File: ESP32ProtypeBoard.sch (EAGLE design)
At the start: 97 parts, among them IC1 SOIC-8, IC2 SI4431BDY, J10 POWER_JACKPTH_LOCK, Q2 MMBT3904, Q3 MMBT3904, U2 ESP-WROOM-32

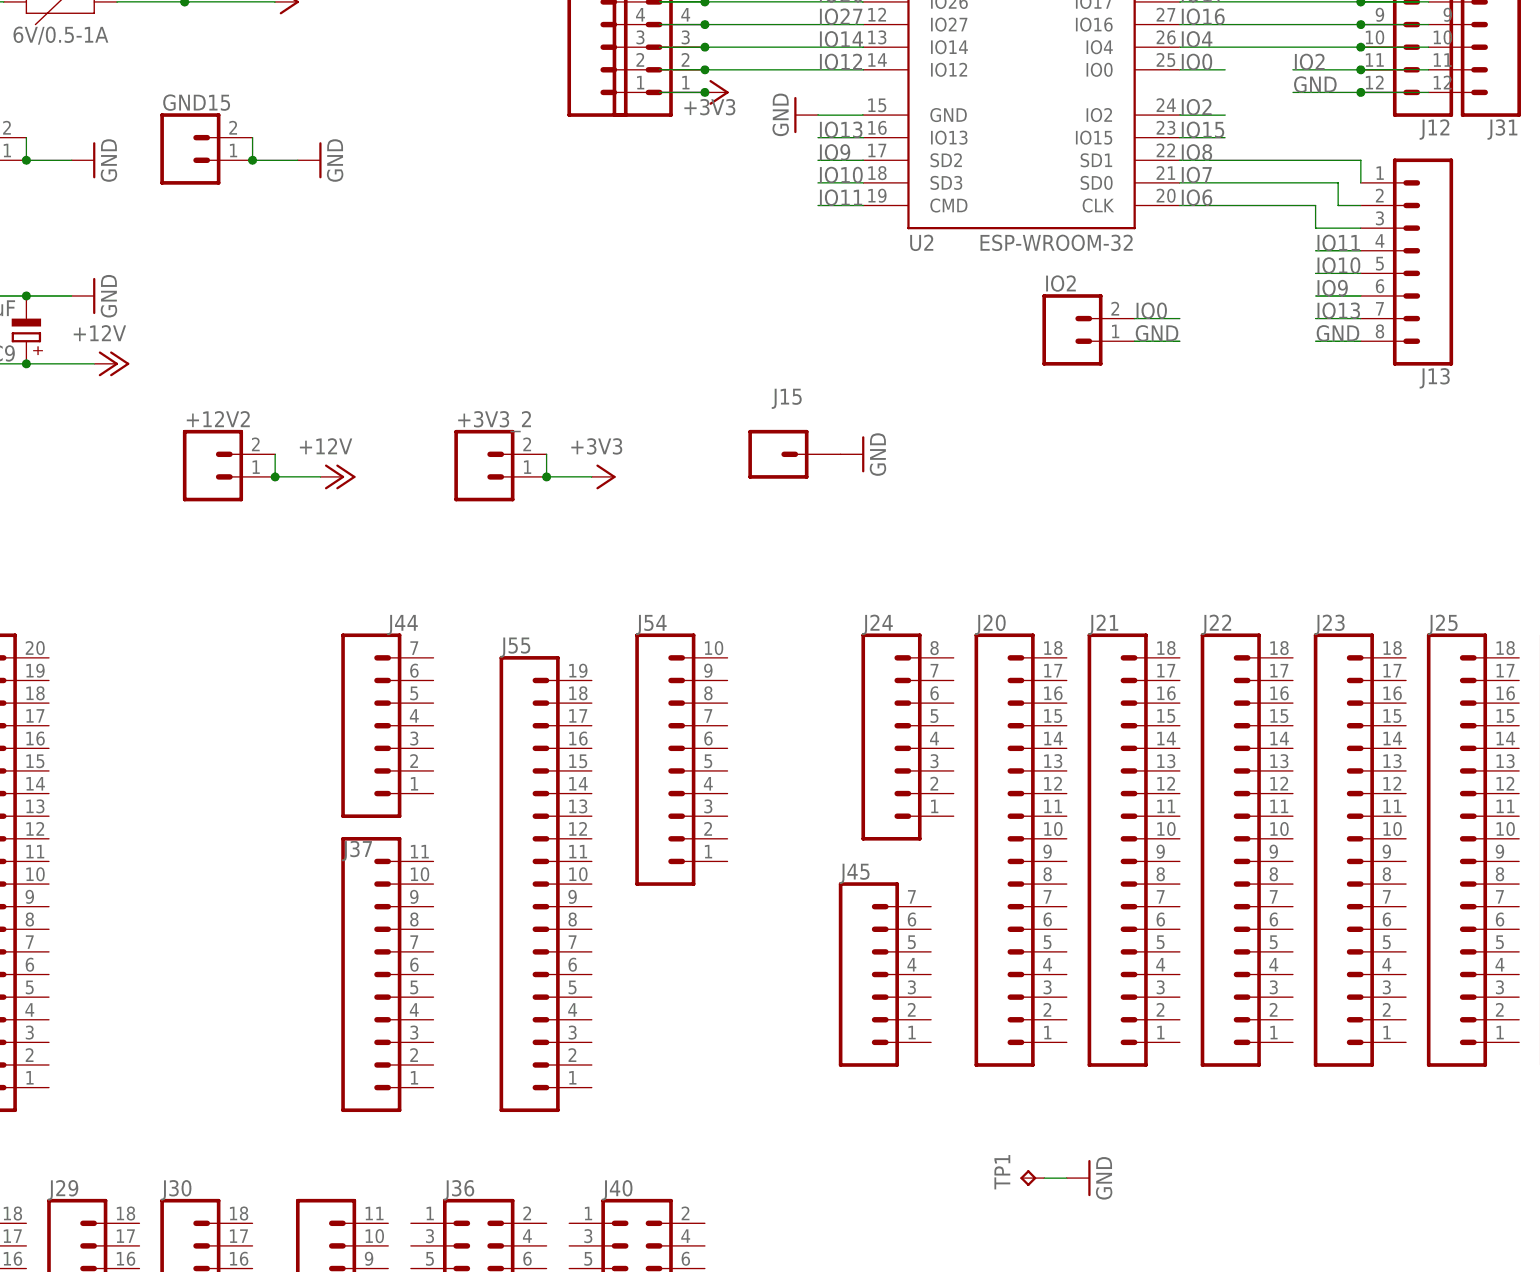
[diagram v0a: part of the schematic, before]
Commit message: Improved wiring of power parts a little, reorganized capacitors
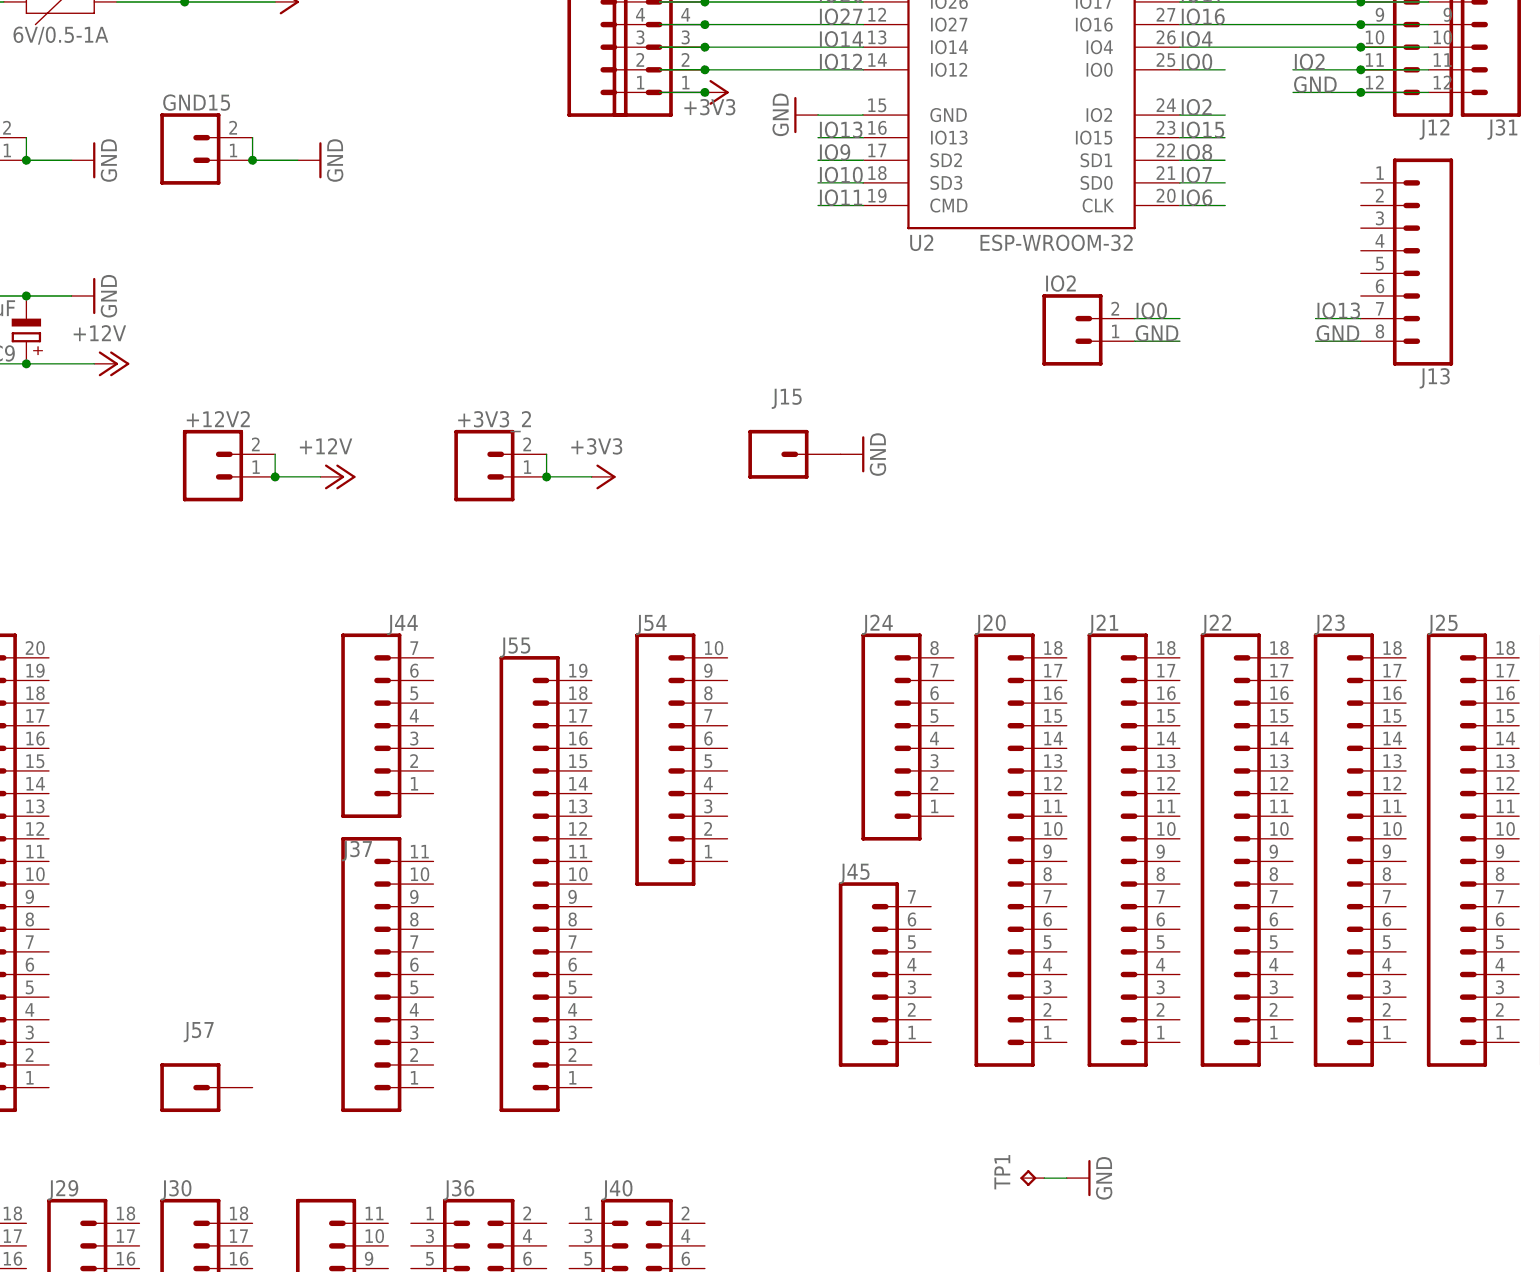
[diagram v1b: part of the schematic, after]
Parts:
- added J57: (no value), SparkFun-Connectors:CONN_01PTH_NO_SILK_KIT
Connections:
- net IO10: no longer J13.5
- net IO11: no longer J13.4
- net IO6: no longer J13.3
- net IO7: no longer J13.2
- net IO8: no longer J13.1
- net IO9: no longer J13.6
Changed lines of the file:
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@@
 <part name="J55" library="SparkFun-Connectors" library_urn="urn:adsk.eagle:library:513" deviceset="CONN_19" device="1X19_NO_SILK" package3d_urn="urn:adsk.eagle:package:38250/1"/>
 <part name="J56" library="SparkFun-Connectors" deviceset="CONN_16" device="1X16_NO_SILK"/>
+<part name="J57" library="SparkFun-Connectors" library_urn="urn:adsk.eagle:library:513" deviceset="CONN_01" device="PTH_NO_SILK_KIT" package3d_urn="urn:adsk.eagle:package:38038/1"/>
 </parts>
 <sheets>
@@
 <attribute name="VALUE" x="-22.86" y="-180.086" size="1.778" layer="96" font="vector"/>
 <attribute name="NAME" x="-22.86" y="-129.032" size="1.778" layer="95" font="vector"/>
+</instance>
+<instance part="J57" gate="G$1" x="104.14" y="-68.58" smashed="yes">
+<attribute name="VALUE" x="104.14" y="-68.326" size="1.778" layer="96" font="vector"/>
+<attribute name="NAME" x="104.14" y="-62.992" size="1.778" layer="95" font="vector"/>
 </instance>
 </instances>
@@
 <pinref part="U2" gate="G$1" pin="SD1"/>
 <label x="215.9" y="35.56" size="1.778" layer="95"/>
-<wire x1="215.9" y1="35.56" x2="236.22" y2="35.56" width="0.1524" layer="91"/>
-<pinref part="J13" gate="G$1" pin="1"/>
-<wire x1="236.22" y1="35.56" x2="236.22" y2="33.02" width="0.1524" layer="91"/>
+<wire x1="215.9" y1="35.56" x2="220.98" y2="35.56" width="0.1524" layer="91"/>
 </segment>
 </net>
@@
 <pinref part="U2" gate="G$1" pin="SD0"/>
 <label x="215.9" y="33.02" size="1.778" layer="95"/>
-<wire x1="215.9" y1="33.02" x2="233.68" y2="33.02" width="0.1524" layer="91"/>
-<wire x1="233.68" y1="33.02" x2="233.68" y2="30.48" width="0.1524" layer="91"/>
-<pinref part="J13" gate="G$1" pin="2"/>
-<wire x1="233.68" y1="30.48" x2="236.22" y2="30.48" width="0.1524" layer="91"/>
+<wire x1="215.9" y1="33.02" x2="220.98" y2="33.02" width="0.1524" layer="91"/>
 </segment>
 </net>
@@
 <pinref part="U2" gate="G$1" pin="CLK"/>
 <label x="215.9" y="30.48" size="1.778" layer="95"/>
-<wire x1="215.9" y1="30.48" x2="231.14" y2="30.48" width="0.1524" layer="91"/>
-<wire x1="231.14" y1="30.48" x2="231.14" y2="27.94" width="0.1524" layer="91"/>
-<pinref part="J13" gate="G$1" pin="3"/>
-<wire x1="231.14" y1="27.94" x2="236.22" y2="27.94" width="0.1524" layer="91"/>
+<wire x1="215.9" y1="30.48" x2="220.98" y2="30.48" width="0.1524" layer="91"/>
 </segment>
 </net>
@@
 <label x="175.26" y="30.48" size="1.778" layer="95"/>
 </segment>
-<segment>
-<pinref part="J13" gate="G$1" pin="4"/>
-<wire x1="236.22" y1="25.4" x2="231.14" y2="25.4" width="0.1524" layer="91"/>
-<label x="231.14" y="25.4" size="1.778" layer="95"/>
-</segment>
 </net>
 <net name="IO10" class="0">
@@
 <label x="175.26" y="33.02" size="1.778" layer="95"/>
 </segment>
-<segment>
-<pinref part="J13" gate="G$1" pin="5"/>
-<wire x1="236.22" y1="22.86" x2="231.14" y2="22.86" width="0.1524" layer="91"/>
-<label x="231.14" y="22.86" size="1.778" layer="95"/>
-</segment>
 </net>
 <net name="IO9" class="0">
@@
 <label x="175.26" y="35.56" size="1.778" layer="95"/>
 </segment>
-<segment>
-<pinref part="J13" gate="G$1" pin="6"/>
-<wire x1="236.22" y1="20.32" x2="231.14" y2="20.32" width="0.1524" layer="91"/>
-<label x="231.14" y="20.32" size="1.778" layer="95"/>
-</segment>
-</net>
+</net>

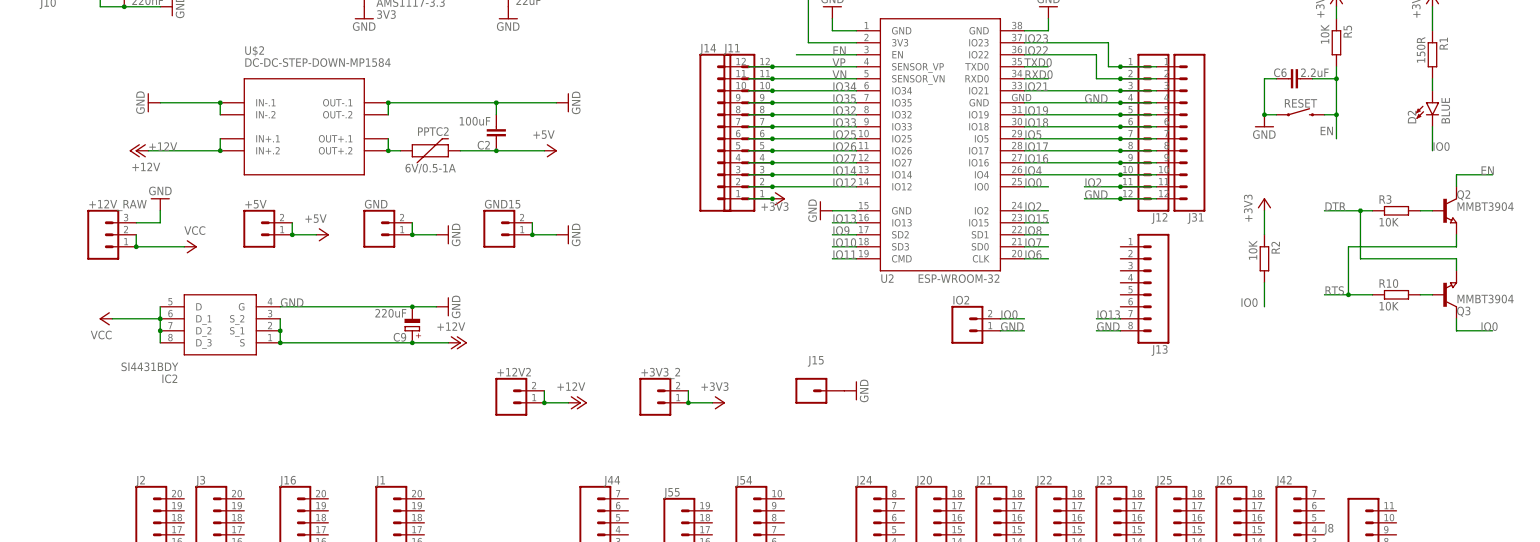
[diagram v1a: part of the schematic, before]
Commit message: Moved input MOSFET, added pwr diode
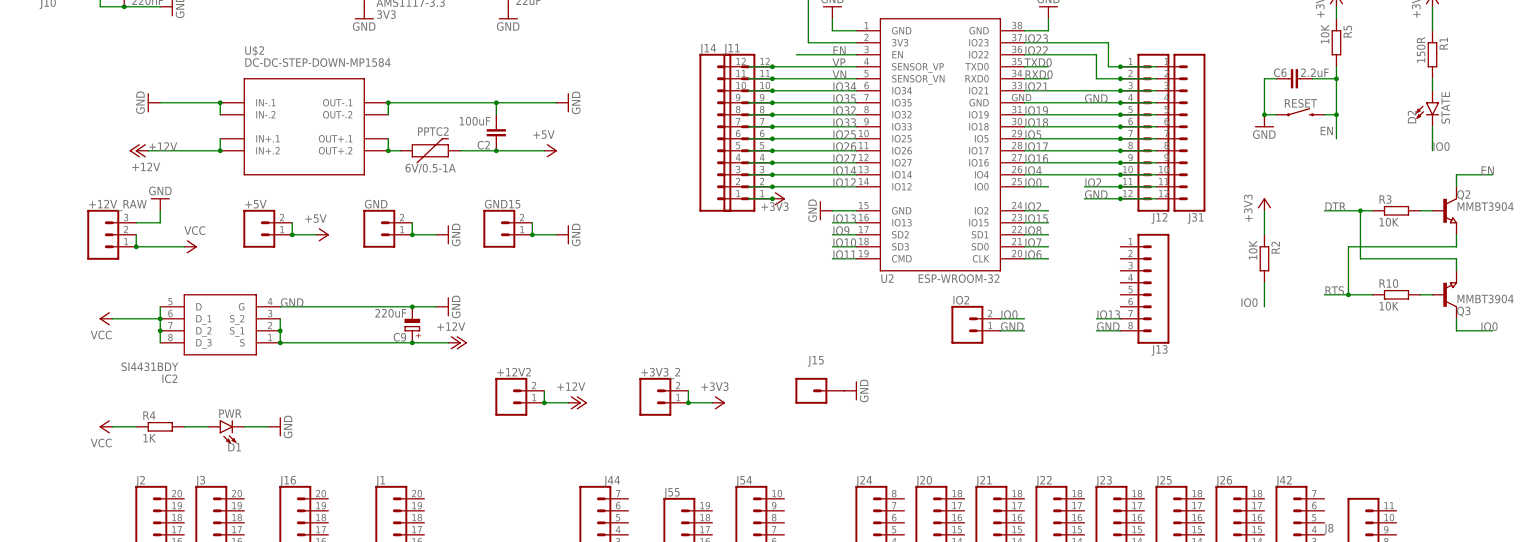
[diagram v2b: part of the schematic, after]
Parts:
- added D1: PWR, SparkFun-LED:LED-GREEN1206
- added R4: 1K, eagle-ltspice:RR1206
- D2: value BLUE -> STATE
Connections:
- new net N$50: D1.A, R4.2
- net GND: now also D1.C
- net VCC: now also R4.1
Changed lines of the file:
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@@
 <part name="P+10" library="supply1" library_urn="urn:adsk.eagle:library:371" deviceset="VCC" device=""/>
 <part name="+3V6" library="supply1" library_urn="urn:adsk.eagle:library:371" deviceset="+3V3" device=""/>
-<part name="D2" library="SparkFun-LED" deviceset="LED-GREEN" device="1206" value="BLUE"/>
+<part name="D2" library="SparkFun-LED" deviceset="LED-GREEN" device="1206" value="STATE"/>
 <part name="R1" library="eagle-ltspice" library_urn="urn:adsk.eagle:library:217" deviceset="R" device="R1206" package3d_urn="urn:adsk.eagle:package:13301/1" value="150R"/>
 <part name="J4" library="SparkFun-Connectors" library_urn="urn:adsk.eagle:library:513" deviceset="CONN_02" device="1X02_NO_SILK" package3d_urn="urn:adsk.eagle:package:38051/1"/>
@@
 <part name="J56" library="SparkFun-Connectors" deviceset="CONN_16" device="1X16_NO_SILK"/>
 <part name="J57" library="SparkFun-Connectors" library_urn="urn:adsk.eagle:library:513" deviceset="CONN_01" device="PTH_NO_SILK_KIT" package3d_urn="urn:adsk.eagle:package:38038/1"/>
+<part name="P+3" library="supply1" library_urn="urn:adsk.eagle:library:371" deviceset="VCC" device=""/>
+<part name="R4" library="eagle-ltspice" library_urn="urn:adsk.eagle:library:217" deviceset="R" device="R1206" package3d_urn="urn:adsk.eagle:package:13301/1" value="1K"/>
+<part name="D1" library="SparkFun-LED" deviceset="LED-GREEN" device="1206" value="PWR"/>
+<part name="GND5" library="supply1" library_urn="urn:adsk.eagle:library:371" deviceset="GND" device=""/>
 </parts>
 <sheets>
@@
 <attribute name="VALUE" x="104.14" y="-68.326" size="1.778" layer="96" font="vector"/>
 <attribute name="NAME" x="104.14" y="-62.992" size="1.778" layer="95" font="vector"/>
+</instance>
+<instance part="P+3" gate="VCC" x="20.32" y="-5.08" smashed="yes" rot="R90">
+<attribute name="VALUE" x="22.86" y="-7.62" size="1.778" layer="96" rot="R180"/>
+</instance>
+<instance part="R4" gate="G$1" x="33.02" y="-5.08" smashed="yes">
+<attribute name="NAME" x="29.21" y="-3.5814" size="1.778" layer="95"/>
+<attribute name="VALUE" x="29.21" y="-8.382" size="1.778" layer="96"/>
+</instance>
+<instance part="D1" gate="G$1" x="45.72" y="-5.08" smashed="yes" rot="R90">
+<attribute name="NAME" x="50.292" y="-8.509" size="1.778" layer="95" font="vector" rot="R180"/>
+<attribute name="VALUE" x="50.292" y="-3.175" size="1.778" layer="96" font="vector" rot="R180" align="top-left"/>
+</instance>
+<instance part="GND5" gate="1" x="58.42" y="-5.08" smashed="yes" rot="R90">
+<attribute name="VALUE" x="60.96" y="-7.62" size="1.778" layer="96" rot="R90"/>
 </instance>
 </instances>
@@
 <wire x1="203.2" y1="-78.74" x2="200.66" y2="-78.74" width="0.1524" layer="91"/>
 </segment>
+<segment>
+<pinref part="D1" gate="G$1" pin="C"/>
+<pinref part="GND5" gate="1" pin="GND"/>
+<wire x1="50.8" y1="-5.08" x2="55.88" y2="-5.08" width="0.1524" layer="91"/>
+</segment>
 </net>
 <net name="+3V3" class="0">
@@
 <wire x1="22.86" y1="17.78" x2="33.02" y2="17.78" width="0.1524" layer="91"/>
 </segment>
+<segment>
+<pinref part="P+3" gate="VCC" pin="VCC"/>
+<pinref part="R4" gate="G$1" pin="1"/>
+<wire x1="22.86" y1="-5.08" x2="27.94" y2="-5.08" width="0.1524" layer="91"/>
+</segment>
 </net>
 <net name="D2A" class="0">
@@
 </segment>
 </net>
+<net name="N$50" class="0">
+<segment>
+<pinref part="R4" gate="G$1" pin="2"/>
+<pinref part="D1" gate="G$1" pin="A"/>
+<wire x1="38.1" y1="-5.08" x2="43.18" y2="-5.08" width="0.1524" layer="91"/>
+</segment>
+</net>
